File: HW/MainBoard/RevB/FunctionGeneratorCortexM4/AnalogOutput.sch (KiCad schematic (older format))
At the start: 39 parts, among them U11 LTC6910, U12 TL072, U13 TL072, U7 MCP601-xOT, U9 TS12A12511DCNR

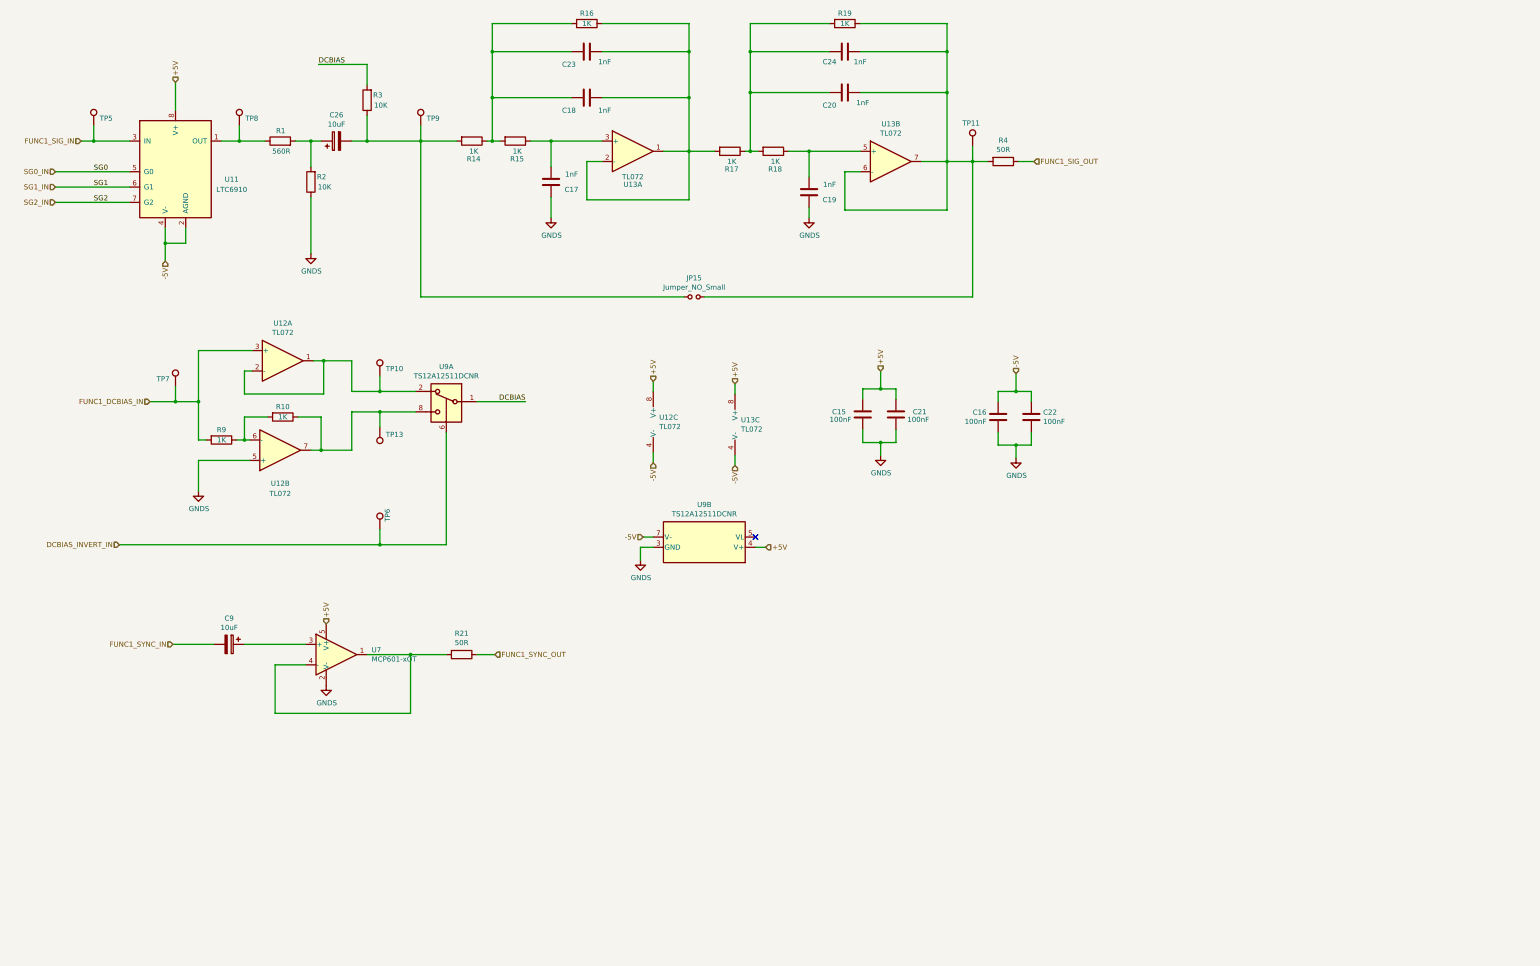
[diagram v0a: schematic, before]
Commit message: Modified PowerSupply section
- Added +2.5V ref
- Added Vin->5V LDO
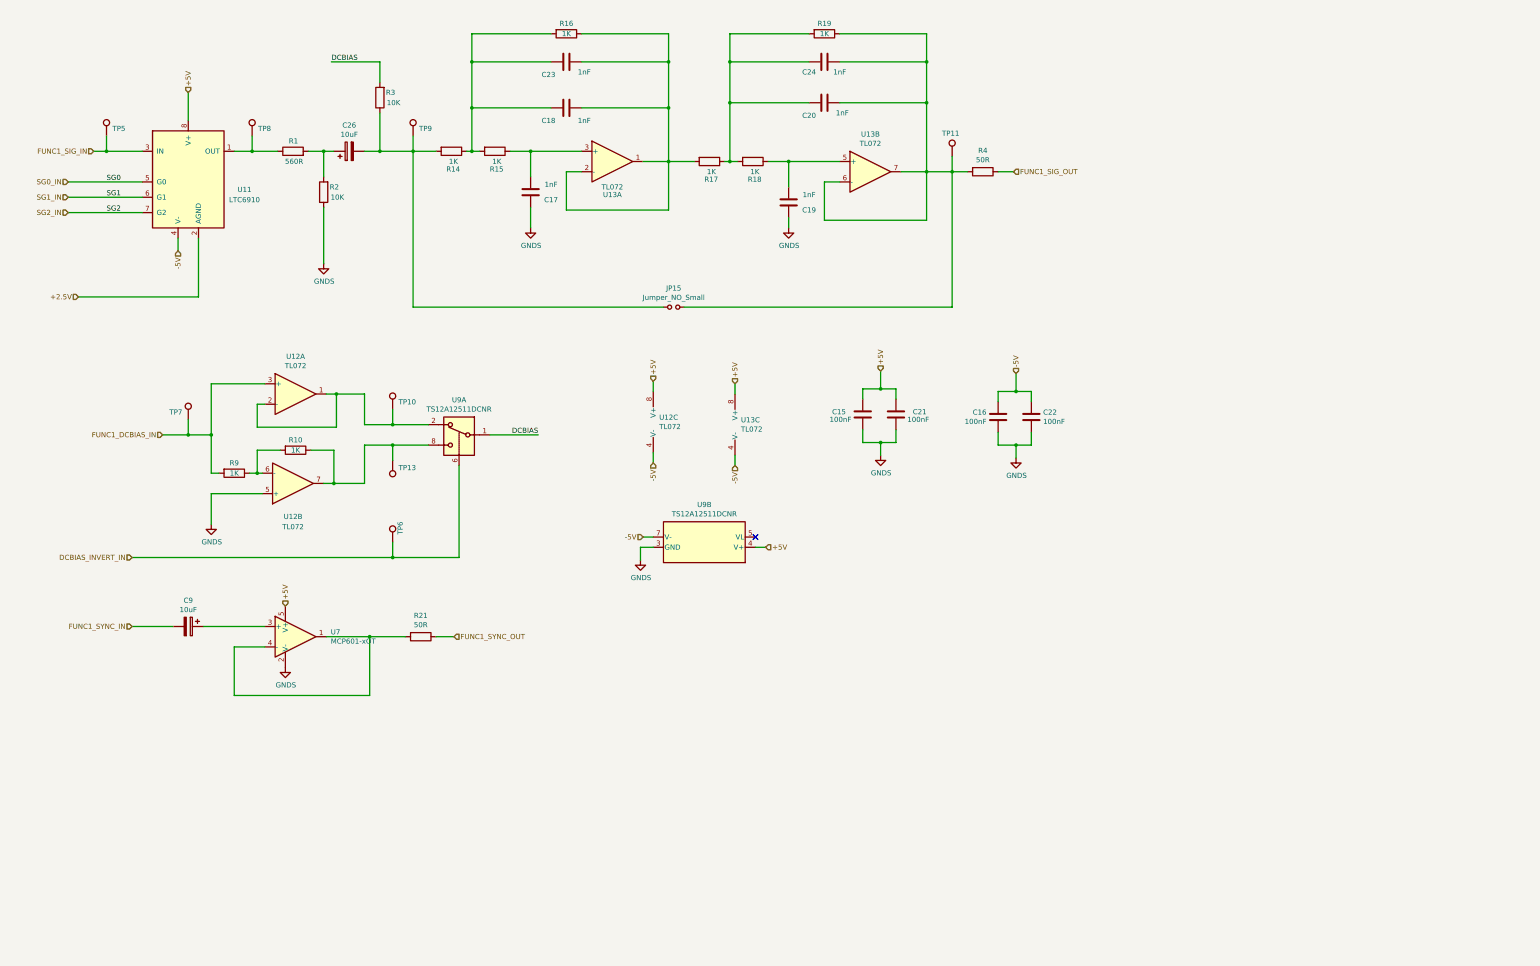
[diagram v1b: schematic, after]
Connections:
- net -5V: no longer U11.2 (AGND)
- new net +2.5V: U11.2 (AGND)
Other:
- moved on the sheet: C17, C18, C19, C20, C23, C24, C26, C9, JP15, R1, R10, R14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

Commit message: REVB DRAFT LAYOUT
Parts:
- added C33, C34: 100nF, Capacitor_SMD:C_1206_3216Metric_Pad1.42x1.75mm_HandSolder, symbol Device:C
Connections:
- net +5V: now also C33.1
- net -5V: now also C34.2
- net GNDS: now also C33.2, C34.1
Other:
- moved on the sheet: C15, C16, C17, C18, C19, C20, C21, C22, C23, C24, C9, JP15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

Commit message: OPTIMIZED REVB LAYOUT
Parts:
- removed C15, C22: 100nF, Capacitor_SMD:C_1206_3216Metric_Pad1.42x1.75mm_HandSolder, symbol Device:C
- added C35, C36: 100nF, Capacitor_SMD:C_1206_3216Metric_Pad1.42x1.75mm_HandSolder, symbol Device:C
- added JP1: Jumper_NC_Small, Jumper:SolderJumper-2_P1.3mm_Bridged_Pad1.0x1.5mm, symbol Device:Jumper_NC_Small
- added JP2, JP4: Jumper_NO_Small, Jumper:SolderJumper-2_P1.3mm_Open_Pad1.0x1.5mm, symbol Device:Jumper_NO_Small
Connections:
- net +2.5V: now also JP1.1; no longer U11.2 (AGND)
- net +5V: now also C34.2, C35.2; no longer C33.1
- net FUNC1_SYNC_IN: now also JP4.1
- net GNDS: now also C35.1, C36.1, JP2.2
- net at R21.2, U7.1, U7.4 (-): now also JP4.2
- net -5V renamed -5V_DCBIAS
- net -5V_DCBIAS: no longer C34.2, U11.4 (V-), U13.4 (V-)
- new net: JP1.2, JP2.1, U11.2 (AGND)
- new net -5V_LPF: C33.1, U13.4 (V-)
- new net -5V_PGA: C36.2, U11.4 (V-)
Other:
- moved on the sheet: C16, C17, C18, C19, C20, C21, C23, C24, C26, C33, C34, C9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

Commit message: Final RevB Layout completed
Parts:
- added C41: 1uF, Capacitor_SMD:C_1206_3216Metric_Pad1.42x1.75mm_HandSolder, symbol Device:C
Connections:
- net +2.5V: now also C41.2
- net GNDS: now also C41.1
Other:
- moved on the sheet: JP2, R10, R9, TP10, TP13, TP6, TP7, U12A, U12B, U9A
